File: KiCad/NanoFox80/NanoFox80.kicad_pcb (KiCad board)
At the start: 2 copper layers, 90 x 37 mm, 66 parts, among them J101 Conn_01x02, J102 Conn_01x02, J111 DB9 Female, J112 Conn_01x02, J113 Conn_01x02, J115 Conn_01x02, P101 ISP/PDI, Q101 BSS84W-7-F, Q102 BSS138W-7-F, SW101 SW_SPST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

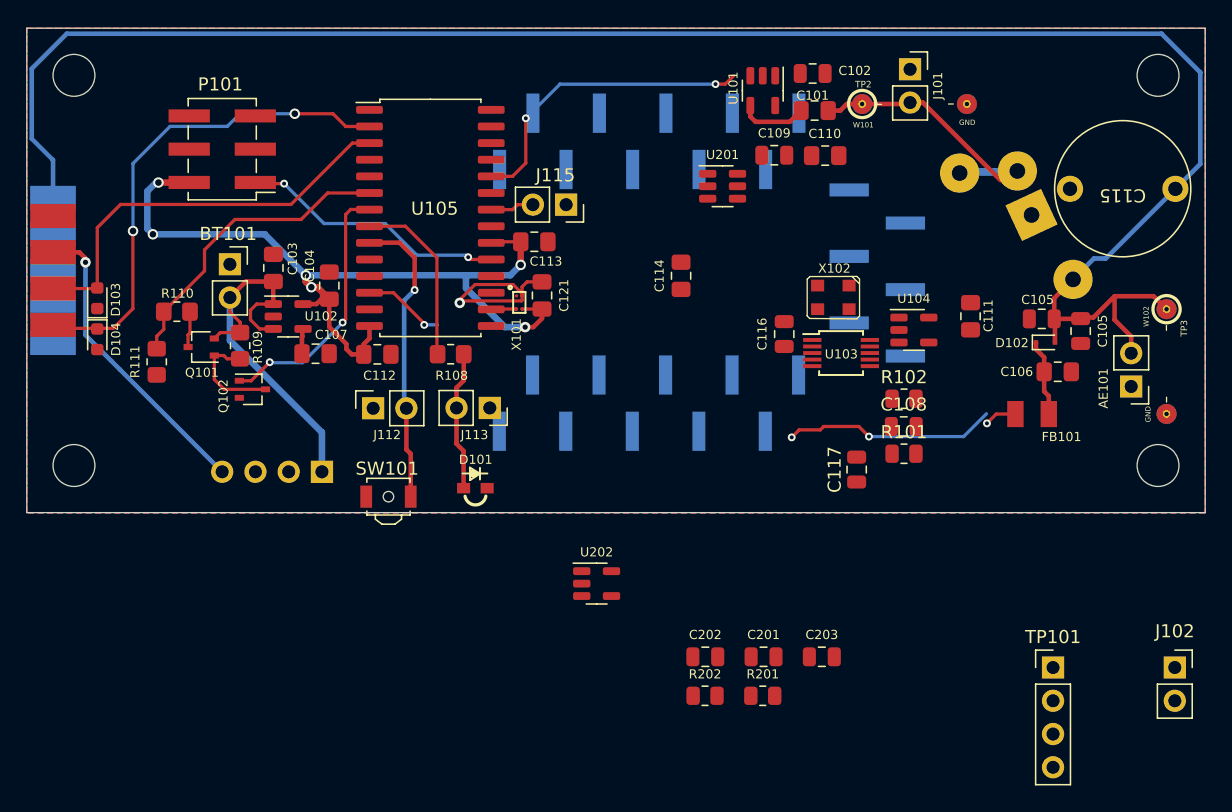
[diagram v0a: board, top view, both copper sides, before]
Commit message: Development
o Fixes to errors in schematic and PCB
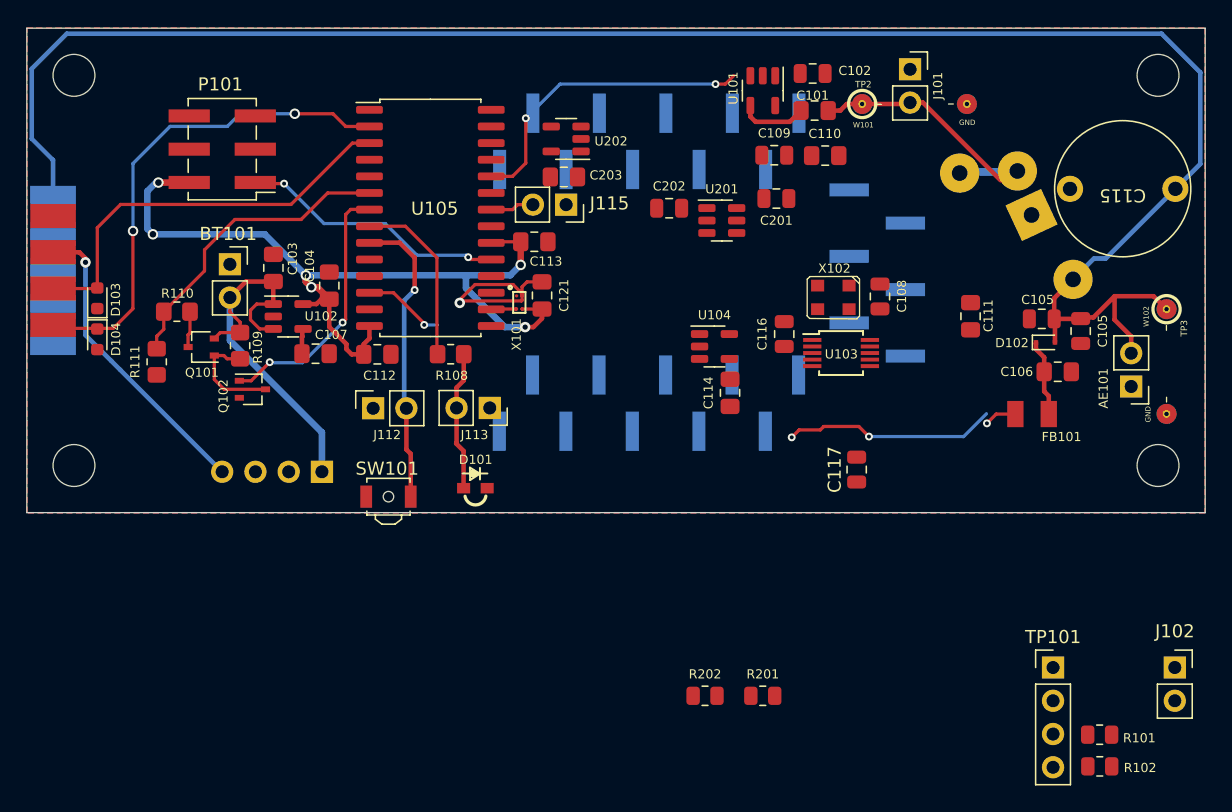
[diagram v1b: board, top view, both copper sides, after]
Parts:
- C203: footprint Capacitor_SMD:C_0805_2012Metric -> Capacitor_SMD:C_0805_2012Metric_Pad1.18x1.45mm_HandSolder
- moved C203 41.6 mm to (121.0, 67.4), turned to 180 degrees
- moved C201 35.0 mm to (137.2, 69.0), turned to 180 degrees
- moved C202 34.4 mm to (129.1, 69.8)
- moved U202 34.0 mm to (121.2, 64.5), turned to 180 degrees
- moved R102 31.8 mm to (161.9, 112.4), turned to 180 degrees
- moved R101 26.1 mm to (161.9, 110.0), turned to 180 degrees
- moved U104 15.3 mm to (132.5, 80.3)
- moved C108 10.1 mm to (145.2, 76.5), turned to 90 degrees
- moved C114 9.69 mm to (133.7, 83.8)
- moved U201 2.62 mm to (133.1, 70.7)
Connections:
- C101 pad 1: GND -> VCC
- C108 pad 1: GND -> VCC
- C109 pad 1: GND -> VCC
- C111 pad 2: GND -> VCC
- C117 pad 2: GND -> VCC
- C203 pad 2: GND -> VCC
- R101 pad 1: GND -> VCC
- R102 pad 1: GND -> VCC
- TP101 pad 2: GND -> VCC
- U101 pad 5: GND -> VCC
- U103 pad 1: GND -> VCC
- U103 pad 7: GND -> VCC
- U104 pad 5: GND -> VCC
- U202 pad 5: GND -> VCC
- X102 pad 4: GND -> VCC
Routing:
- net unconnected-(MOD201-Pad2): track 0.00 -> 23.7 mm, vias 0 -> 2
- net Enable_RF: track 23.7 -> 0.00 mm, vias 2 -> 0

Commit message: Update NanoFox80.kicad_pcb
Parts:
- moved R201 11.9 mm to (134.0, 95.2)
- moved R202 11.8 mm to (129.1, 95.5)
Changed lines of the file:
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@@
     (property "Sheetfile" "NanoFox80.kicad_sch")
     (property "Sheetname" "")
+    (solder_mask_margin 0.06)
+    (clearance 0.06)
     (attr smd)
     (fp_text reference "U101" (at -0.19 2.25 -90) (layer "F.SilkS")
@@
     (property "Sheetfile" "wifi_module.kicad_sch")
     (property "Sheetname" "WiFi_Module")
+    (solder_mask_margin 0.06)
+    (clearance 0.06)
     (attr smd)
     (fp_text reference "U201" (at 0 -2.4) (layer "F.SilkS")
@@
   )
   (footprint "Resistor_SMD:R_0805_2012Metric" (layer "F.Cu")
-    (at 131.8 106.99)
+    (at 129.08 95.52)
     (descr "Resistor SMD 0805 (2012 Metric), square (rectangular) end terminal, IPC_7351 nominal, (Body size source: IPC-SM-782 page 72, https://www.pcb-3d.com/wordpress/wp-content/uploads/ipc-sm-782a_amendment_1_and_2.pdf), generated with kicad-footprint-generator")
     (tags "resistor")
@@
   )
   (footprint "Resistor_SMD:R_0805_2012Metric" (layer "F.Cu")
-    (at 136.21 106.99)
+    (at 133.98 95.25)
     (descr "Resistor SMD 0805 (2012 Metric), square (rectangular) end terminal, IPC_7351 nominal, (Body size source: IPC-SM-782 page 72, https://www.pcb-3d.com/wordpress/wp-content/uploads/ipc-sm-782a_amendment_1_and_2.pdf), generated with kicad-footprint-generator")
     (tags "resistor")
@@
     (property "Sheetfile" "wifi_module.kicad_sch")
     (property "Sheetname" "WiFi_Module")
+    (solder_mask_margin 0.06)
+    (clearance 0.06)
     (attr smd)
     (fp_text reference "U202" (at -3.43 -0.17) (layer "F.SilkS")
@@
     (property "Sheetfile" "NanoFox80.kicad_sch")
     (property "Sheetname" "")
-    (solder_mask_margin 0.07)
-    (clearance 0.2)
+    (solder_mask_margin 0.06)
+    (clearance 0.06)
     (attr smd)
     (fp_text reference "U102" (at 2.52 -0.02) (layer "F.SilkS")

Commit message: Development
PCB Updates
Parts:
- removed J102: Conn_01x02, Connector_PinSocket_2.54mm:PinSocket_1x02_P2.54mm_Vertical
- moved TP101 45.4 mm to (126.2, 72.8)
- moved R101 45.4 mm to (129.8, 77.9)
- moved R102 45.4 mm to (129.8, 80.3)
- moved R201 40.4 mm to (114.1, 60.1)
- moved C117 31.9 mm to (132.7, 59.6), turned to 0 degrees
- moved R202 23.3 mm to (129.2, 72.2)
- moved C109 18.3 mm to (147.4, 80.8)
- moved C110 16.9 mm to (133.7, 81.0)
- moved C101 16.2 mm to (137.8, 75.5), turned to 90 degrees
- moved C114 9.24 mm to (133.5, 74.6), turned to 180 degrees
- moved U104 2.81 mm to (133.6, 77.7), turned to 90 degrees
- moved C102 2.68 mm to (140.2, 59.6)
- moved W102 1.72 mm to (167.9, 76.0)
- moved C203 0.82 mm to (121.0, 66.5)
- moved C201 0.75 mm to (137.1, 69.7)
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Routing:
- net Net-(FB101-Pad2): track 25.0 -> 58.7 mm, vias 4 -> 2
- net +BATT: track 31.6 -> 63.9 mm, vias 0 -> 2
- net Net-(R102-Pad2): track 0.00 -> 30.8 mm, vias 0 -> 1
- net Net-(R101-Pad2): track 0.00 -> 27.1 mm, vias 0 -> 1
- net WIFI_ENABLE: track 0.00 -> 26.3 mm
- net unconnected-(MOD201-Pad2): track 23.7 -> 0.00 mm, vias 2 -> 0
- net ~{WIFI_RESET}: track 0.00 -> 12.1 mm, vias 0 -> 1
- net WiFi Module Detect: track 0.00 -> 7.55 mm
- net Net-(C201-Pad2): track 0.00 -> 6.69 mm, vias 0 -> 1
- net VCC: track 0.00 -> 5.51 mm
- net WIFI_TX: track 0.00 -> 4.78 mm
- net Net-(C102-Pad2): track 5.24 -> 1.99 mm
- net Net-(C102-Pad1): track 15.9 -> 17.3 mm
- net Antenna: track 142.4 -> 143.0 mm

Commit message: Development
PCB changes
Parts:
- moved J112 2.20 mm to (104.3, 85.2)
- moved J113 2.12 mm to (113.3, 85.3)
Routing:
- net +BATT: track 63.9 -> 99.4 mm
- net Net-(D101-Pad2): track 10.7 -> 12.6 mm
- net Net-(J112-Pad2): track 22.7 -> 24.4 mm
- net Net-(FB101-Pad2): track 58.7 -> 58.1 mm
- net +3V3: vias 6 -> 5

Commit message: Development
PCB Changes
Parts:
- moved C111 22.6 mm to (129.6, 75.8), turned to 0 degrees
- moved C101 9.80 mm to (141.9, 84.5), turned to -90 degrees
- moved W101 1.78 mm to (144.1, 60.0)
- moved C109 1.53 mm to (147.3, 82.3)
- moved R102 1.26 mm to (129.7, 81.6)
- moved R101 0.77 mm to (129.7, 78.7)
- moved TP101 0.11 mm to (126.1, 72.8)
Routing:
- net VCC: track 5.51 -> 91.1 mm, vias 0 -> 2
- net GND: track 13.5 -> 92.1 mm, vias 1 -> 22
- net WiFi Module Detect: track 7.55 -> 55.6 mm, vias 0 -> 1
- net Net-(U101-Pad1): track 0.00 -> 37.9 mm
- net Net-(U101-Pad2): track 0.00 -> 31.4 mm, vias 0 -> 2
- net Enable_RF: track 0.00 -> 29.4 mm, vias 0 -> 2
- net Net-(MOD201-Pad20): track 0.00 -> 28.7 mm, vias 0 -> 1
- net WIFI_RX: track 0.00 -> 24.5 mm, vias 0 -> 3
- net Net-(R102-Pad2): track 30.8 -> 53.2 mm
- net Net-(R101-Pad2): track 27.1 -> 45.2 mm
- net ~{WIFI_RESET}: track 12.1 -> 21.1 mm, vias 1 -> 2
- net Net-(C116-Pad2): track 0.00 -> 2.94 mm
- net Net-(C116-Pad1): track 0.00 -> 2.14 mm
- net Net-(C114-Pad1): track 0.00 -> 1.99 mm
- net +BATT: track 99.4 -> 101.2 mm
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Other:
- board text added: "NanoFox80 Rev: 10-July-2022"
- board text removed: "Fout"
- board text removed: "NanoFox80 Rev: 4-July-2022"
- board text removed: "U101-Out"

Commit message: Development
Small PCB tweaks
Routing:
- net Net-(C102-Pad1): track 17.6 -> 15.2 mm
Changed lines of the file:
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@@
     )
     (fp_line (start -1.33 0) (end -1.33 -1.33) (layer "F.SilkS") (width 0.12))
-    (fp_line (start -1.33 1.27) (end -1.33 8.95) (layer "F.SilkS") (width 0.12))
-    (fp_line (start 1.33 1.27) (end 1.33 8.95) (layer "F.SilkS") (width 0.12))
     (fp_line (start -1.33 1.27) (end 1.33 1.27) (layer "F.SilkS") (width 0.12))
     (fp_line (start -1.33 -1.33) (end 0 -1.33) (layer "F.SilkS") (width 0.12))
+    (fp_line (start 1.33 1.27) (end 1.33 8.95) (layer "F.SilkS") (width 0.12))
+    (fp_line (start -1.33 1.27) (end -1.33 8.95) (layer "F.SilkS") (width 0.12))
     (fp_line (start -1.33 8.95) (end 1.33 8.95) (layer "F.SilkS") (width 0.12))
+    (fp_line (start -1.26 9) (end 1.26 9) (layer "F.CrtYd") (width 0.05))
+    (fp_line (start 1.26 9) (end 1.26 -1.28) (layer "F.CrtYd") (width 0.05))
+    (fp_line (start -1.26 -1.28) (end -1.26 9) (layer "F.CrtYd") (width 0.05))
     (fp_line (start 1.26 -1.28) (end -1.26 -1.28) (layer "F.CrtYd") (width 0.05))
-    (fp_line (start 1.28 9) (end 1.26 -1.28) (layer "F.CrtYd") (width 0.05))
-    (fp_line (start -1.26 -1.28) (end -1.26 9) (layer "F.CrtYd") (width 0.05))
-    (fp_line (start -1.26 9) (end 1.26 9) (layer "F.CrtYd") (width 0.05))
+    (fp_line (start 1.27 8.89) (end -1.27 8.89) (layer "F.Fab") (width 0.1))
+    (fp_line (start -0.635 -1.27) (end 1.27 -1.27) (layer "F.Fab") (width 0.1))
     (fp_line (start 1.27 -1.27) (end 1.27 8.89) (layer "F.Fab") (width 0.1))
     (fp_line (start -1.27 8.89) (end -1.27 -0.635) (layer "F.Fab") (width 0.1))
     (fp_line (start -1.27 -0.635) (end -0.635 -1.27) (layer "F.Fab") (width 0.1))
-    (fp_line (start -0.635 -1.27) (end 1.27 -1.27) (layer "F.Fab") (width 0.1))
-    (fp_line (start 1.27 8.89) (end -1.27 8.89) (layer "F.Fab") (width 0.1))
     (pad "1" thru_hole rect (at 0 0) (size 1.7 1.7) (drill 1) (layers *.Cu *.Mask)
       (net 1 "GND") (pinfunction "Pin_1") (pintype "passive"))
@@
   (segment (start 102.54 89.88) (end 116.81 89.88) (width 0.5) (layer "B.Cu") (net 2))
   (segment (start 142.92 59.61) (end 141.2175 59.61) (width 0.35) (layer "F.Cu") (net 3))
-  (segment (start 151.7 64.94) (end 153.31 64.94) (width 0.35) (layer "F.Cu") (net 3))
-  (segment (start 153.31 64.94) (end 155.275 66.905) (width 0.35) (layer "F.Cu") (net 3))
   (segment (start 143.35 60.04) (end 142.92 59.61) (width 0.35) (layer "F.Cu") (net 3))
+  (segment (start 149.365 67.065) (end 151.2475 67.065) (width 0.35) (layer "F.Cu") (net 3))
   (segment (start 145.87 61.79) (end 147.35 61.79) (width 0.35) (layer "F.Cu") (net 3))
   (segment (start 147.35 61.79) (end 147.46 61.68) (width 0.35) (layer "F.Cu") (net 3))
-  (segment (start 155.275 66.905) (end 155.6575 66.905) (width 0.35) (layer "F.Cu") (net 3))
+  (segment (start 147.46 65.16) (end 149.365 67.065) (width 0.35) (layer "F.Cu") (net 3))
   (segment (start 144.12 60.04) (end 143.35 60.04) (width 0.35) (layer "F.Cu") (net 3))
+  (segment (start 147.46 61.68) (end 147.46 65.16) (width 0.35) (layer "F.Cu") (net 3))
   (segment (start 144.12 60.04) (end 145.87 61.79) (width 0.35) (layer "F.Cu") (net 3))
-  (segment (start 148.44 61.68) (end 151.7 64.94) (width 0.35) (layer "F.Cu") (net 3))
-  (segment (start 147.46 61.68) (end 148.44 61.68) (width 0.35) (layer "F.Cu") (net 3))
   (segment (start 139.1425 59.61) (end 137.1825 59.61) (width 0.25) (layer "F.Cu") (net 4))
   (segment (start 137.1825 59.61) (end 137.16 59.6325) (width 0.25) (layer "F.Cu") (net 4))

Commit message: Development
PCB Updates
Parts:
- moved C117 0.63 mm to (132.8, 60.3)
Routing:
- net GND: track 92.1 -> 364.4 mm, vias 22 -> 197
- net Net-(R102-Pad2): track 53.2 -> 54.2 mm
- net Net-(R108-Pad1): track 13.5 -> 12.6 mm
- net VCC: track 91.1 -> 91.9 mm
- net Net-(U101-Pad1): track 37.9 -> 37.4 mm

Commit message: Development
PCB silkscreen change
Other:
- board text removed: "FT-50-67 FT-82-67"
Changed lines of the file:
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@@
   )
   (gr_rect (start 80 56) (end 170 93) (layer "Edge.Cuts") (width 0.1) (fill none))
-  (gr_text "FT-50-67\nFT-82-67" (at 158.25 58.69) (layer "B.SilkS")
-    (effects (font (size 1 1) (thickness 0.15)) (justify mirror))
-  )
   (gr_text "NanoFox80\nRev: 10-July-2022" (at 96.11 64.54) (layer "B.SilkS")
     (effects (font (size 1.5 1.5) (thickness 0.3)) (justify mirror))
